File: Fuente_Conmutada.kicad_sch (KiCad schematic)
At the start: 48 parts, among them J1 Terminal_220v, J2 Terminal_12v, J3 Vout, Q1 IRF840, Q2 IRF840, T1 Transformer_1P_SS, U1 TL494, U2 IR2110

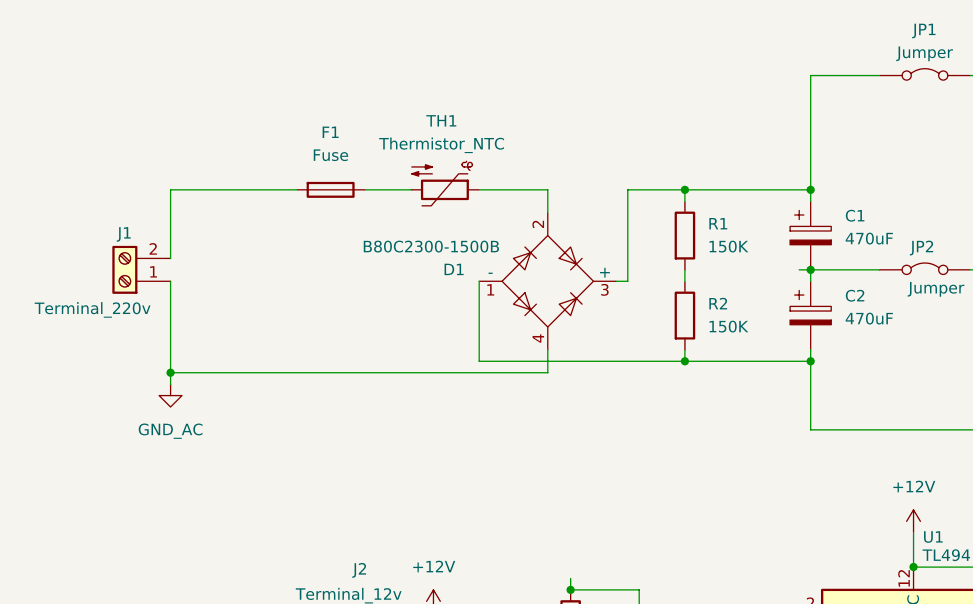
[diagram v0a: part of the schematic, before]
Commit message: Footprints correctos agregados
- Hice y puse el footprint del transformador
- Corregí algunos otros footprints como el del puente de diodos por el que tenemos realmente y el portafusible
- Actualicé los componentes eso en el editor de PCB y puse un cuadrado de 10x10cm donde se hace el PCB
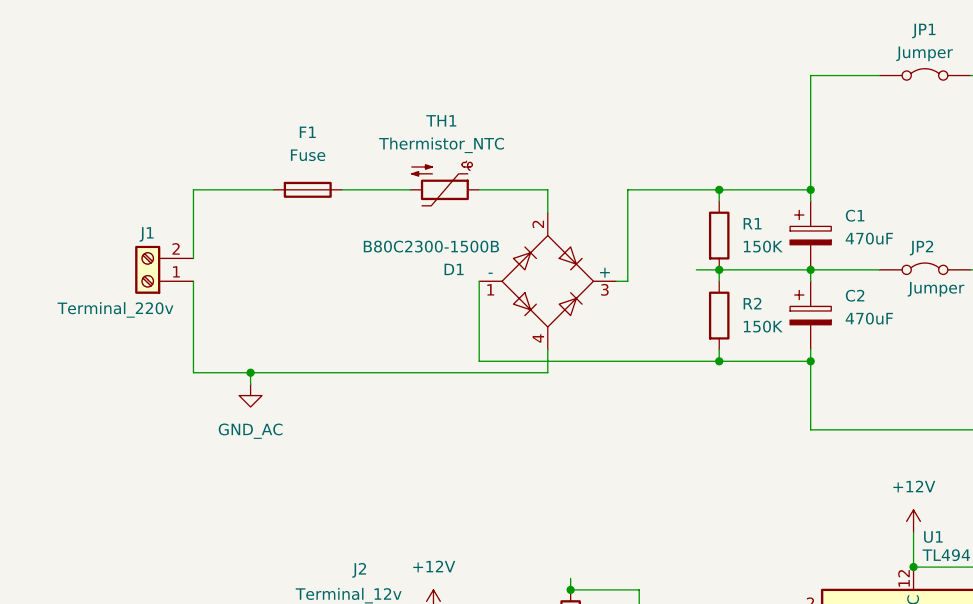
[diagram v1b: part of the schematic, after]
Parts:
- D1: footprint Diode_THT:Diode_Bridge_Round_D9.8mm -> Diode_THT:Diode_Bridge_Vishay_KBPM
- F1: footprint Fuse:Fuse_SunFuse-6HP -> Fuse:Fuseholder_Cylinder-5x20mm_Stelvio-Kontek_PTF78_Horizontal_Open
- L1: footprint Inductor_THT:L_Radial_D18.0mm_P10.00mm -> Inductor_THT:L_Toroid_Vertical_L22.4mm_W10.2mm_P7.90mm_Vishay_TJ4
- T1: footprint Transformer_THT:Transformer_Breve_TEZ-28x33 -> TransformerLib:Ferrite_Core_Trans
- TH1: footprint Resistor_THT:R_Axial_DIN0309_L9.0mm_D3.2mm_P12.70mm_Horizontal -> Resistor_THT:R_Axial_DIN0207_L6.3mm_D2.5mm_P7.62mm_Horizontal
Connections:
- net at C1.2, C2.1, JP2.1 (A): now also R1.2, R2.1
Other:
- moved on the sheet: F1, J1, R1, R2
